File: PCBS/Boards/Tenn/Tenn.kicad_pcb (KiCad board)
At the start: 2 copper layers, 90 x 25 mm, 59 parts, among them J1 Conn_01x02_Socket, J15 Conn_01x03_Male, J18 Conn_01x30_Pin, SW2 SW_Push, SW3 SW_Push, SW4 SW_SPDT, U2 DRV8871DDA, U3 DRV8871DDA

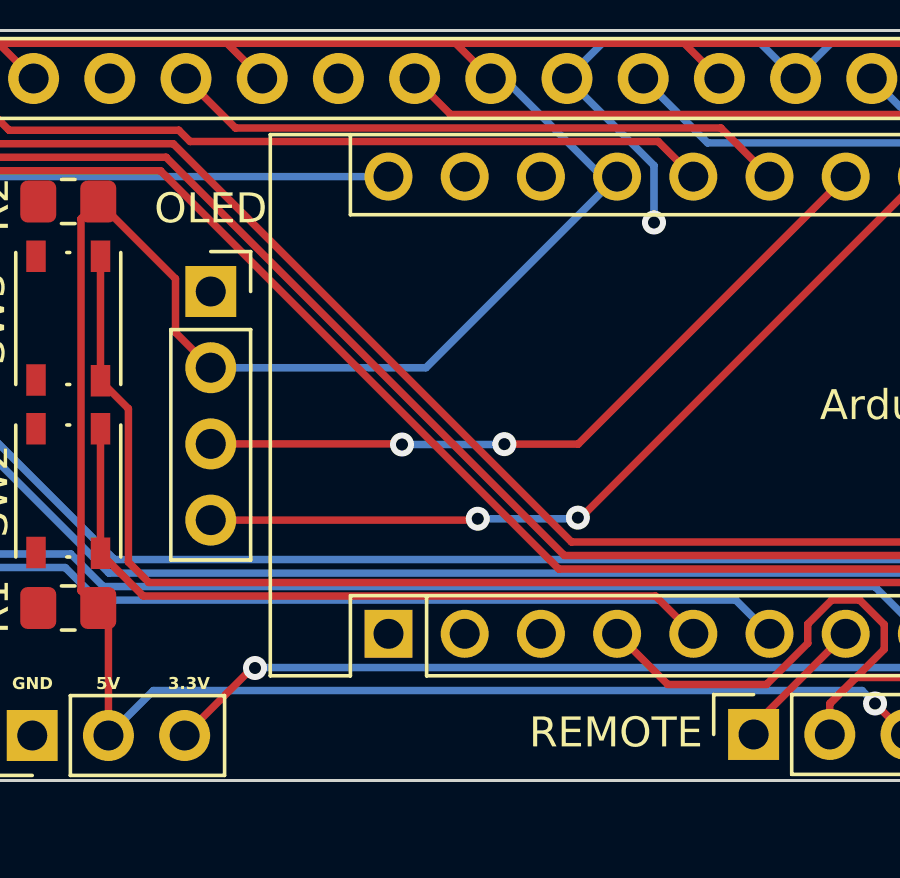
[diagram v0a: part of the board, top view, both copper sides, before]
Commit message: updates production files of tenn board
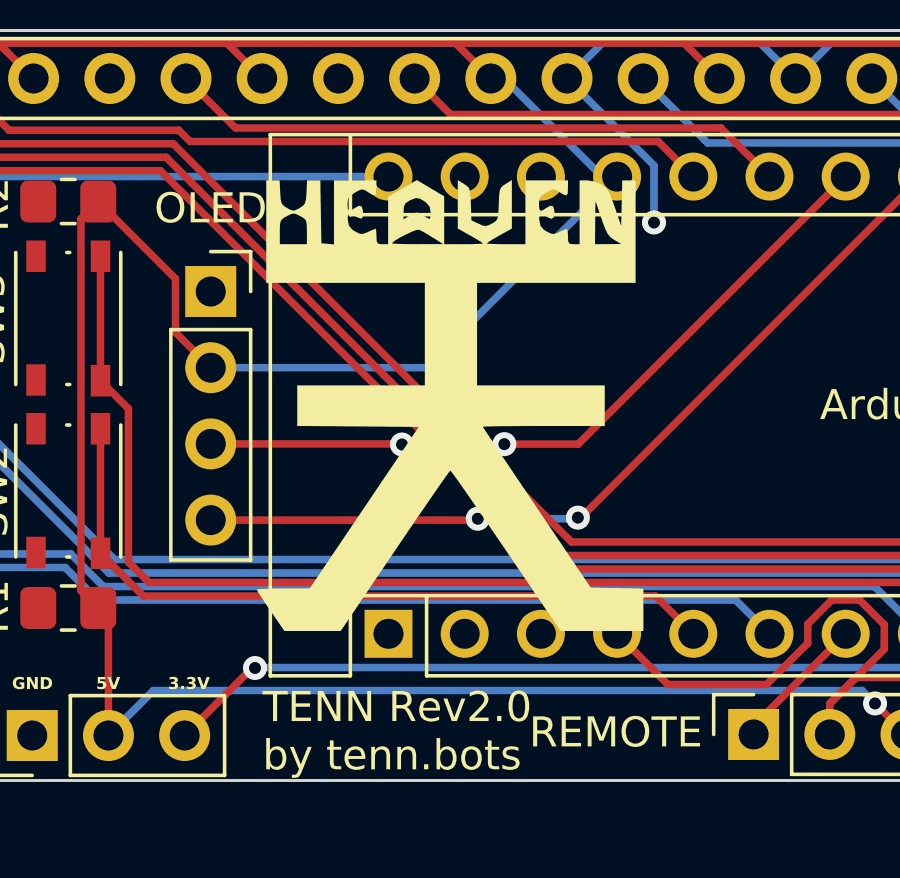
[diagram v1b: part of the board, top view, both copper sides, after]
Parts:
- added 5V: LOGO, LOGO, B.Cu at (124.0, 93.0)
- added ANALOG IN: LOGO, LOGO, B.Cu at (124.0, 109.0)
- added DIGITAL IN: LOGO, LOGO, B.Cu at (124.0, 104.0)
- added G***: LOGO, LOGO, F.Cu at (152.0, 99.5)
- added G***: LOGO, LOGO, B.Cu at (167.2, 99.5)
- added GND: LOGO, LOGO, B.Cu at (124.0, 99.0)
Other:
- board text added: "TENN Rev2.0 by tenn.bots"

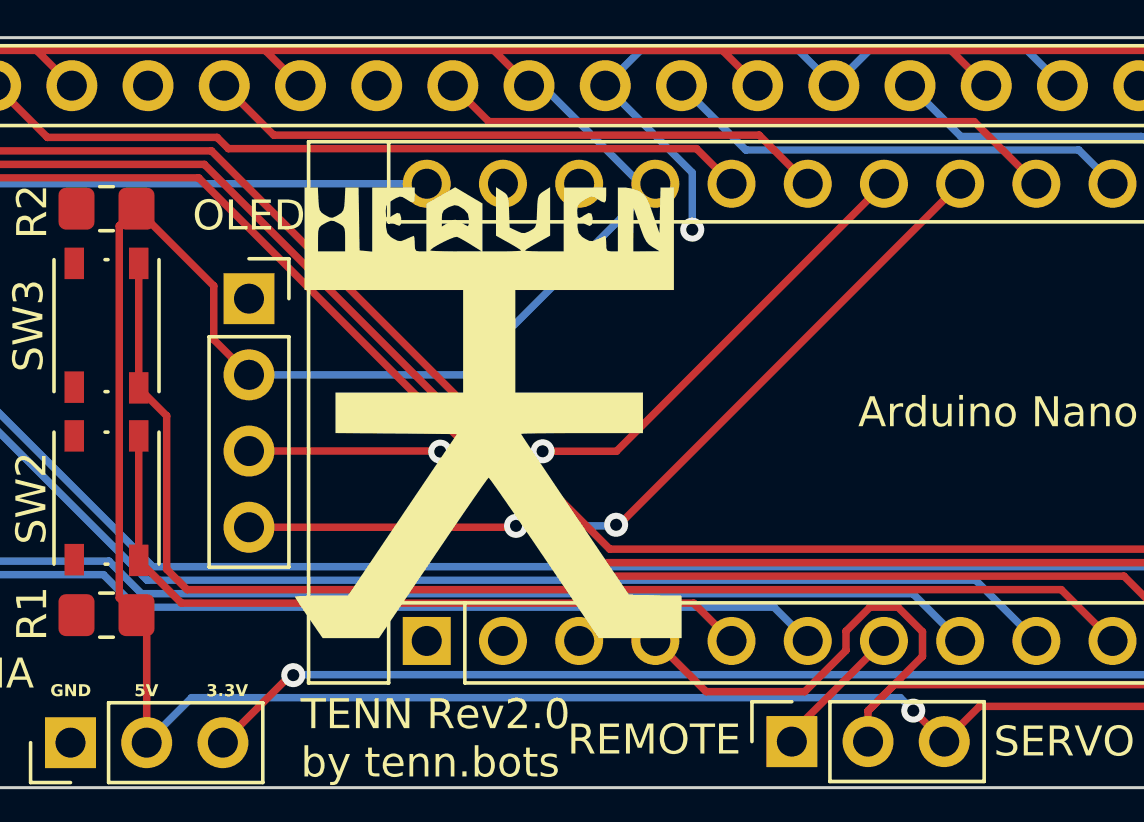
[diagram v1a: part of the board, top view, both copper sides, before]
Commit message: updates jucad tenn board file, now OLED screen pins are in the correct orientation
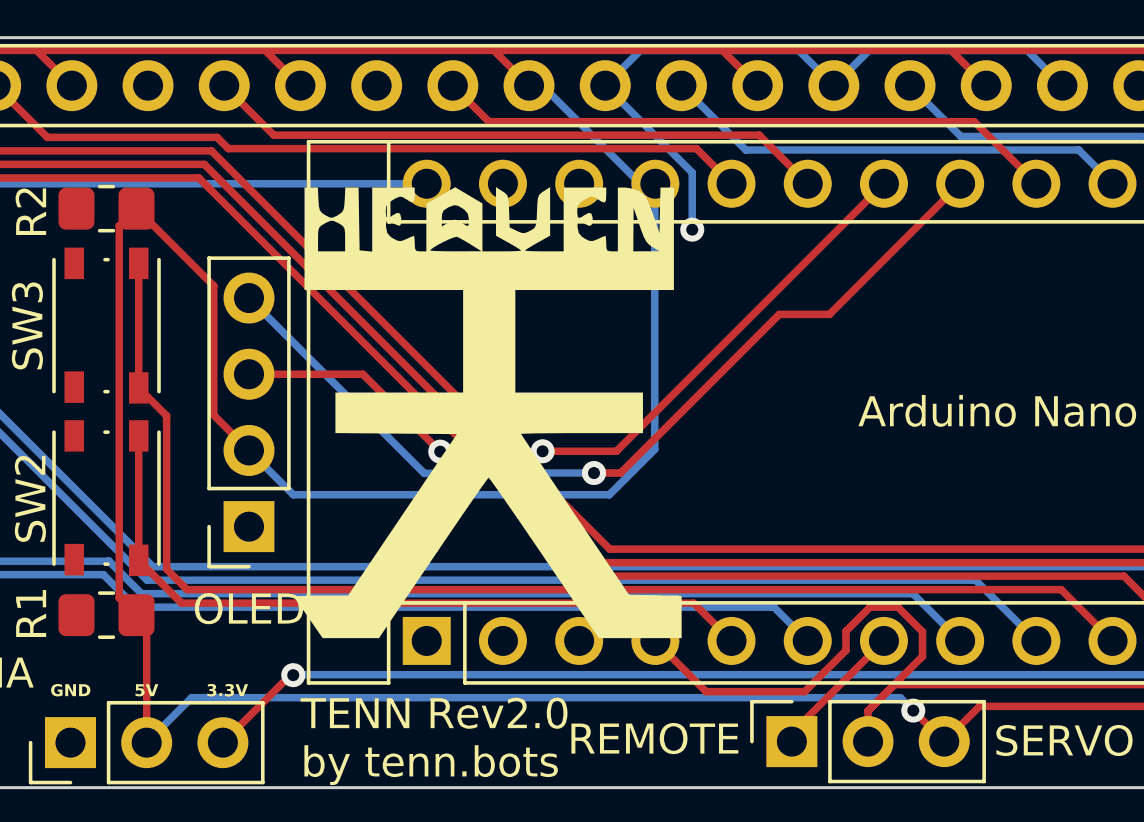
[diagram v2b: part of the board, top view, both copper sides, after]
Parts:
- moved OLED 7.60 mm to (144.0, 103.3), turned to 180 degrees
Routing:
- net +5V: track 169.6 -> 179.5 mm
- net SDA: track 28.4 -> 30.1 mm, vias 2 -> 1
- net SCL: track 24.9 -> 25.9 mm

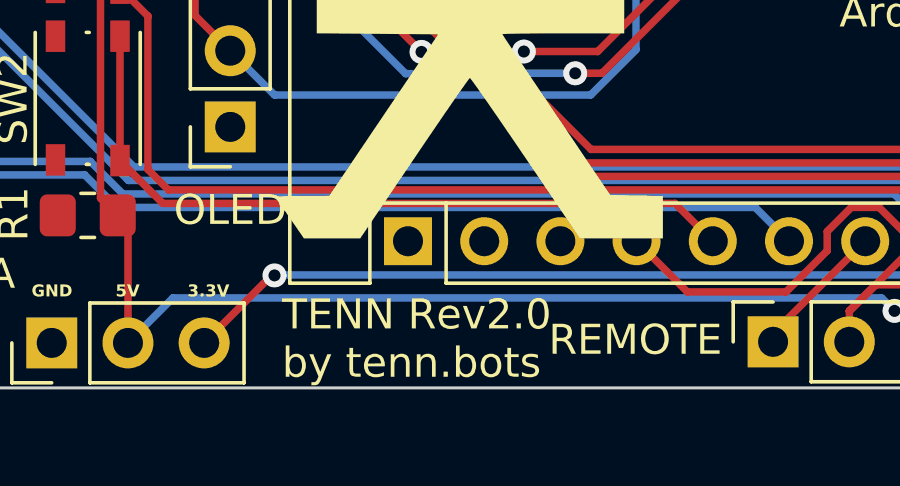
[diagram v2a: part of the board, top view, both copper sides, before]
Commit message: changes revision of tenn board from 2.0 to 2.1
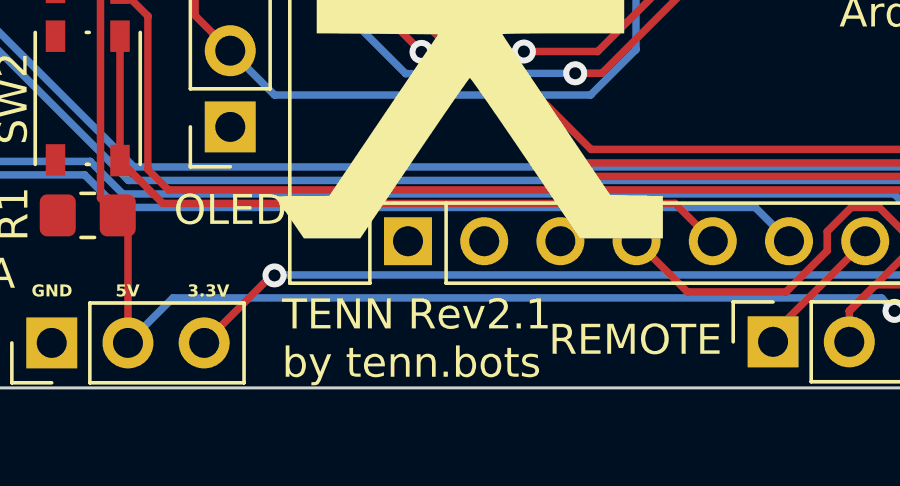
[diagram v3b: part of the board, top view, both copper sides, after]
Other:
- board text added: "TENN Rev2.1 by tenn.bots"
- board text removed: "TENN Rev2.0 by tenn.bots"
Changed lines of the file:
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@@
 		)
 		(fp_text user "${REFERENCE}"
-			(at 0 3.81 270)
+			(at 0 3.81 -90)
 			(layer "F.Fab")
 			(effects
@@
 		)
 	)
-	(gr_text "TENN Rev2.0\nby tenn.bots"
+	(gr_text "TENN Rev2.1\nby tenn.bots"
 		(at 145.75 111.75 0)
 		(layer "F.SilkS")

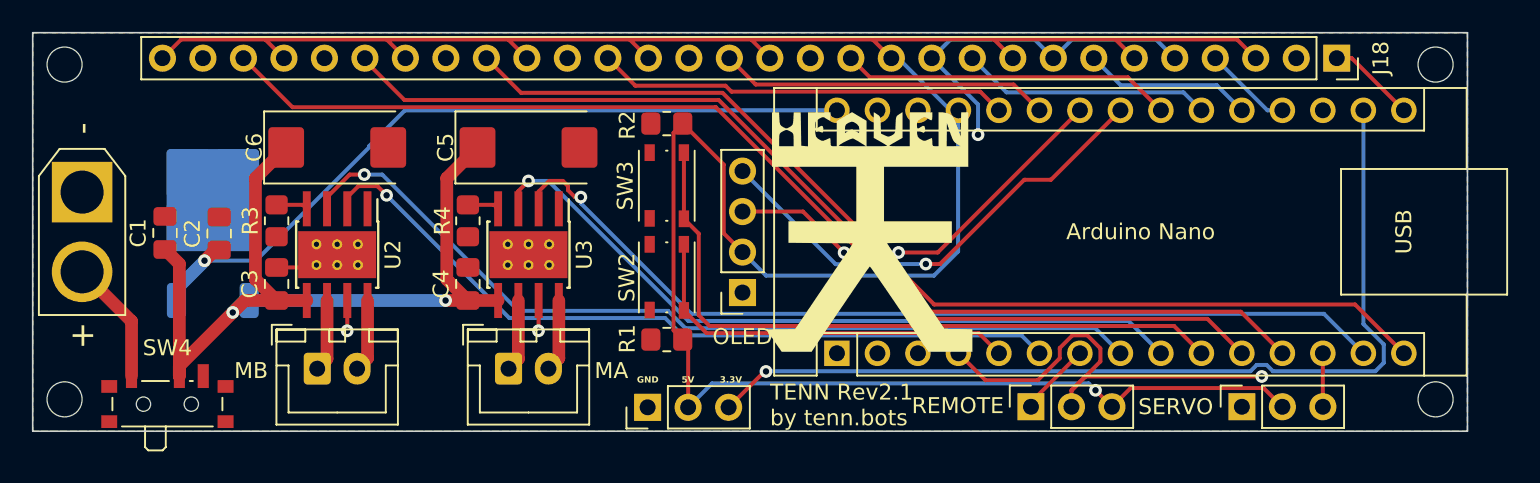
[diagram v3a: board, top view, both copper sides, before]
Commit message: Updates footprints in tenn.pcb, changes cap tantulum to 0805
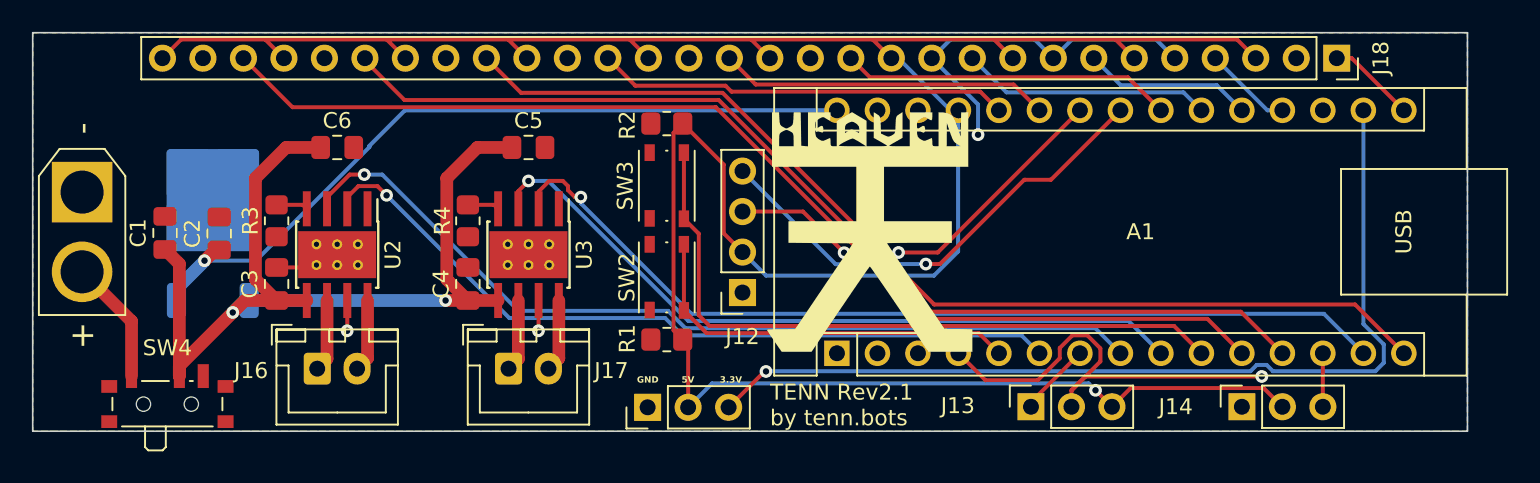
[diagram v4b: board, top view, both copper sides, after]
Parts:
- removed REF** (x4): MountingHole_2.2mm_M2_ISO7380, MountingHole:MountingHole_2.2mm_M2_ISO7380
- A1: renamed from Arduino Nano
- C5, C6: footprint Capacitor_Tantalum_SMD:CP_EIA-7343-31_Kemet-D_Pad2.25x2.55mm_HandSolder -> Capacitor_SMD:C_0805_2012Metric_Pad1.18x1.45mm_HandSolder
- renumbered OLED to J12, REMOTE to J13, SERVO to J14, MB to J16, MA to J17, L7085/StepDownModule to U1
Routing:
- net VM: track 57.8 -> 62.1 mm
